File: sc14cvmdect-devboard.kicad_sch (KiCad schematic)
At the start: 32 parts, among them J1 Conn_01x08, J2 USB_C_Receptacle_USB2.0_16P, J3 Conn_01x03, J4 Conn_01x18, J6 Conn_01x18, SW1 SW_Push, U1 TLV1117LV33, U2 SC14CVMDECT, U3 FT230XQ

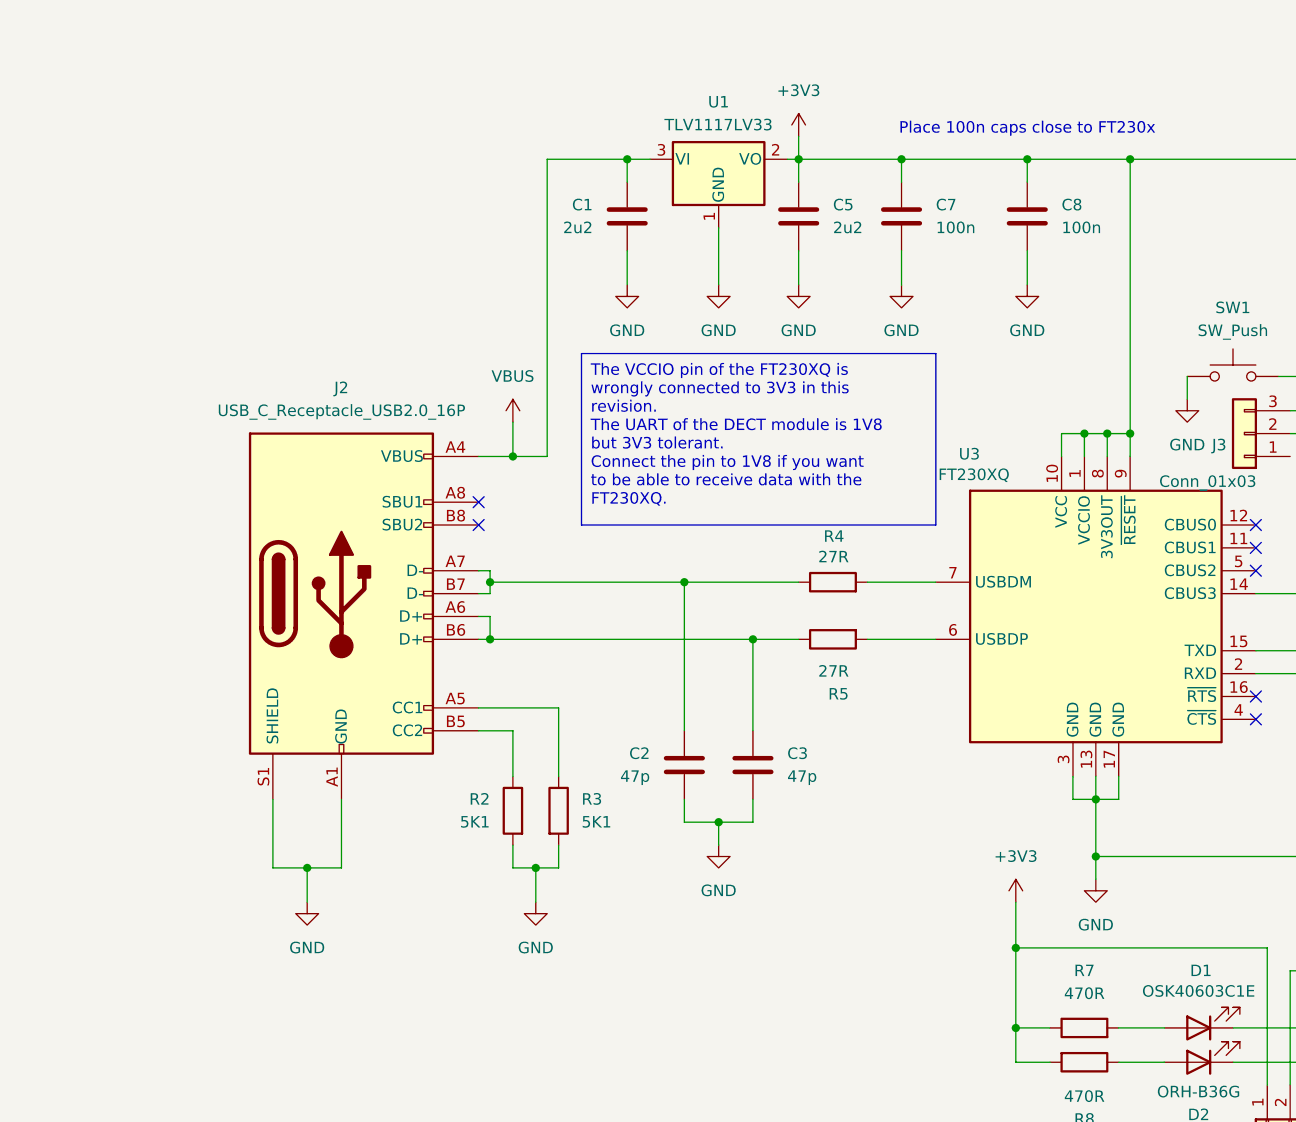
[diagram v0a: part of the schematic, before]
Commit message: Add 1V8 voltage regulator to fix internal UART voltage.
This commits adds a voltage regulator to change the voltage at the
VCCIO pin of the internal UART converter to 1V8.
This design was not tested in production/hardware yet but instead
is a hot fix to offer an alternative to the manufacturing of boards
with the wrong UART voltage.
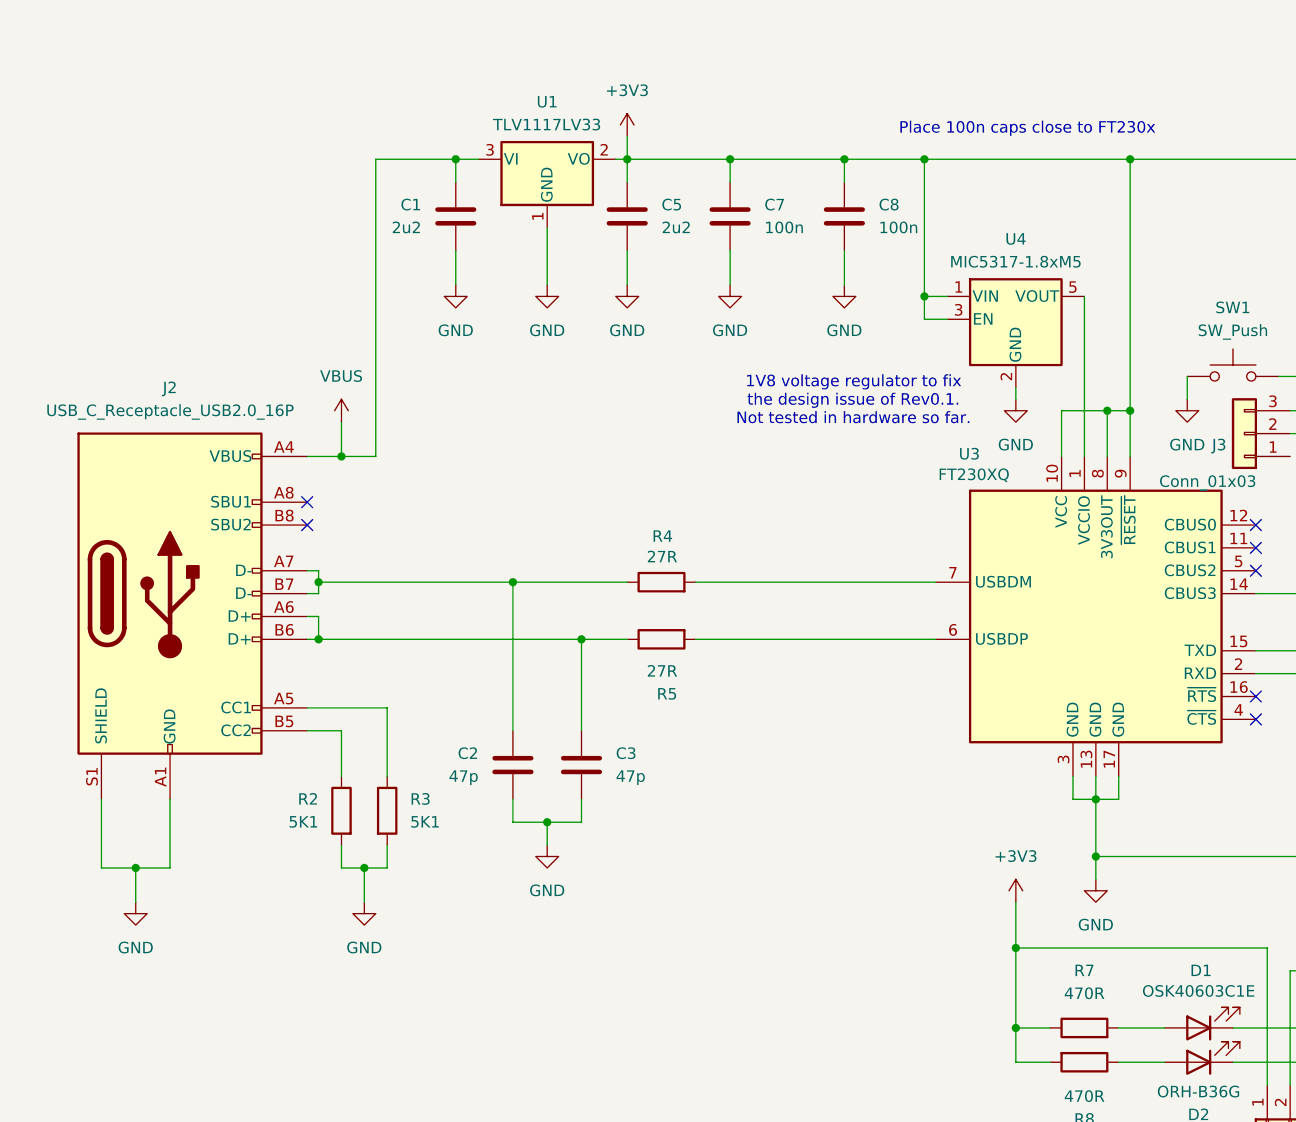
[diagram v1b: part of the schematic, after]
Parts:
- added U4: MIC5317-1.8xM5, Package_TO_SOT_SMD:SOT-23-5, symbol Regulator_Linear:MIC5317-1.8xM5
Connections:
- net +3V3: now also U4.1 (VIN), U4.3 (EN); no longer U3.1 (VCCIO)
- net GND: now also U4.2 (GND)
- new net: U3.1 (VCCIO), U4.5 (VOUT)
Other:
- note added: "1V8 voltage regulator to fix the design issue of Rev0.1. Not tested in hardware so far."
- moved on the sheet: C1, C2, C3, C5, C7, C8, J2, R2, R3, R4, R5, U1

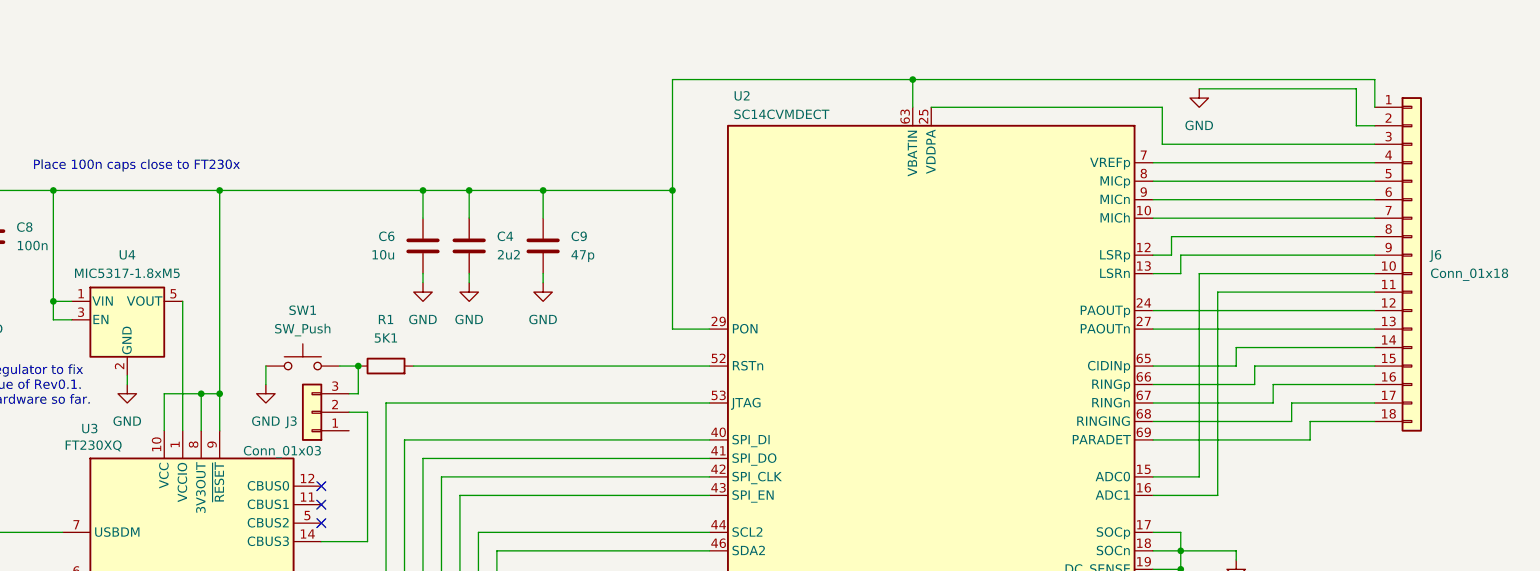
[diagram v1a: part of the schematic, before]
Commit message: tweaks
Added
 - +1V8 on left pinheader
 - VBUS on left pinheader

Moved RESET Button up a little
Moved Jumper up a little
Moved right pinheaders by 1.27mm so they match a standard raster
breadboard
Replaced fancy pin labels with readable labels
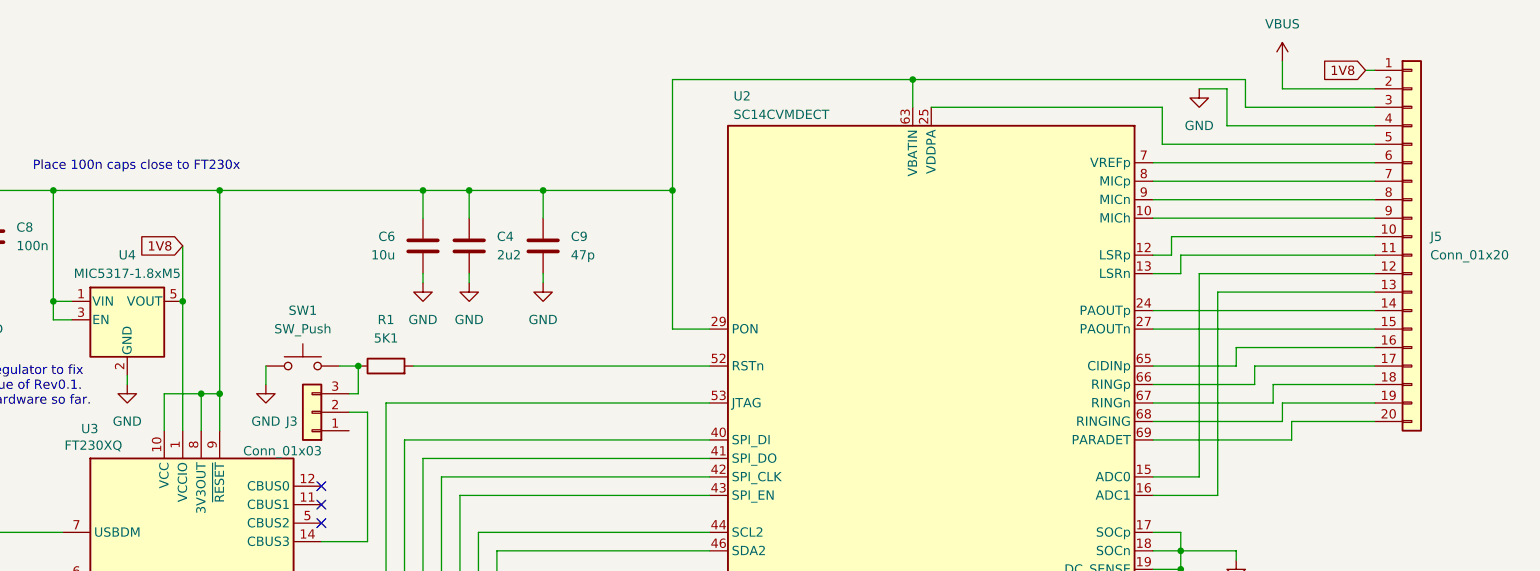
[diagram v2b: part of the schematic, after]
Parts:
- removed J6: Conn_01x18, Connector_PinHeader_2.54mm:PinHeader_1x18_P2.54mm_Vertical, symbol Connector_Generic:Conn_01x18
- added J5: Conn_01x20, Connector_PinHeader_2.54mm:PinHeader_1x20_P2.54mm_Vertical, symbol Connector_Generic:Conn_01x20
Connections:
- net +3V3: now also J5.3 (Pin_3)
- net GND: now also J5.4 (Pin_4)
- net VBUS: now also J5.2 (Pin_2)
- net 1V8: now reaches U3.1 (VCCIO), U4.5 (VOUT)
- net 1V8: now also J5.1 (Pin_1)
- net at U2.15 (ADC0): now also J5.12 (Pin_12)
- net at U2.16 (ADC1): now also J5.13 (Pin_13)
- net at U2.24 (PAOUTp): now also J5.14 (Pin_14)
- net at U2.27 (PAOUTn): now also J5.15 (Pin_15)
- net at U2.65 (CIDINp): now also J5.16 (Pin_16)
- net at U2.66 (RINGp): now also J5.17 (Pin_17)
- net at U2.67 (RINGn): now also J5.18 (Pin_18)
- net at U2.68 (RINGING): now also J5.19 (Pin_19)
- net at U2.69 (PARADET): now also J5.20 (Pin_20)
- net at U2.25 (VDDPA): now also J5.5 (Pin_5)
- net at U2.7 (VREFp): now also J5.6 (Pin_6)
- net at U2.8 (MICp): now also J5.7 (Pin_7)
- net at U2.9 (MICn): now also J5.8 (Pin_8)
- net at U2.10 (MICh): now also J5.9 (Pin_9)
- net at U2.12 (LSRp): now also J5.10 (Pin_10)
- net at U2.13 (LSRn): now also J5.11 (Pin_11)
